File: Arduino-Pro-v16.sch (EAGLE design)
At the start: 42 parts, among them IC1 ATMEGA1281-16AU

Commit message: Added FTDI 3.3V programmer
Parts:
- added C4: (no value), SparkFun-Capacitors:CAP0603-CAP
- added J1: FTDI Basic Programmer, SparkFun-Connectors:ARDUINO_SERIAL_PROGRAMPTH
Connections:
- removed net VCCA: PCB1.5V@2, PCB1.5V@4
- new net DTR: C4.2, J1.DTR
- new net RXI: IC1.(RXD1/INT2)PD2, J1.TXO
- new net TX0: IC1.(TXD1/INT3)PD3, J1.RXI
- net 3V3: now also J1.VCC, PCB1.3V3@1, PCB1.3V3@17
- net 5VMISO: now also JP3.1
- net 5VMOSI: now also JP3.4
- net 5VROV: now also PCB1.5V@2, PCB1.5V@4
- net 5VSCK: now also JP3.3
- net GND: now also J1.CTS, J1.GND
- net MISO: no longer JP3.1
- net MOSI: no longer JP3.4
- net RESET: now also C4.1
- net SCK: no longer JP3.3
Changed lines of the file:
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@@
 <part name="U$1" library="DiscreteComponents" deviceset="SWITCH" device=""/>
 <part name="JTAG_CONNECTOR" library="Connectors" deviceset="MICRO-FIT-4-SMD" device="" technology="-PART"/>
+<part name="3V1" library="SparkFun-Aesthetics" deviceset="VCCA" device=""/>
+<part name="3V4" library="SparkFun-Aesthetics" deviceset="VCCA" device=""/>
+<part name="J1" library="SparkFun-Connectors" deviceset="ARDUINO_SERIAL_PROGRAM" device="PTH" value="FTDI Basic Programmer"/>
+<part name="C4" library="SparkFun-Capacitors" deviceset="CAP" device="0603-CAP"/>
 </parts>
 <sheets>
@@
 <instance part="U$1" gate="G$1" x="-218.44" y="149.86" rot="R90"/>
 <instance part="JTAG_CONNECTOR" gate="G$1" x="-104.14" y="43.18" rot="R270"/>
+<instance part="3V1" gate="G$1" x="302.26" y="127" smashed="yes"/>
+<instance part="3V4" gate="G$1" x="342.9" y="119.38" smashed="yes"/>
+<instance part="J1" gate="G$1" x="137.16" y="137.16"/>
+<instance part="C4" gate="G$1" x="-231.14" y="160.02" rot="R270"/>
 </instances>
 <busses>
@@
 <wire x1="-218.44" y1="142.24" x2="-218.44" y2="139.7" width="0.1524" layer="91"/>
 </segment>
+<segment>
+<pinref part="J1" gate="G$1" pin="GND"/>
+<wire x1="142.24" y1="144.78" x2="147.32" y2="144.78" width="0.1524" layer="91"/>
+<label x="142.24" y="144.78" size="1.778" layer="95"/>
+</segment>
+<segment>
+<pinref part="J1" gate="G$1" pin="CTS"/>
+<wire x1="142.24" y1="142.24" x2="147.32" y2="142.24" width="0.1524" layer="91"/>
+<label x="142.24" y="142.24" size="1.778" layer="95"/>
+</segment>
 </net>
 <net name="RESET" class="0">
@@
 <wire x1="-218.44" y1="160.02" x2="-218.44" y2="157.48" width="0.1524" layer="91"/>
 <junction x="-218.44" y="160.02"/>
+<pinref part="C4" gate="G$1" pin="1"/>
+<wire x1="-226.06" y1="160.02" x2="-218.44" y2="160.02" width="0.1524" layer="91"/>
 </segment>
 </net>
 <net name="SCK" class="0">
-<segment>
-<wire x1="30.48" y1="144.78" x2="15.24" y2="144.78" width="0.1524" layer="91"/>
-<label x="15.24" y="144.78" size="1.778" layer="95"/>
-<pinref part="JP3" gate="G$1" pin="3"/>
-</segment>
 <segment>
 <pinref part="SPI_PIN" gate="G$1" pin="4"/>
@@
 <net name="MISO" class="0">
 <segment>
-<wire x1="30.48" y1="147.32" x2="15.24" y2="147.32" width="0.1524" layer="91"/>
-<label x="15.24" y="147.32" size="1.778" layer="95"/>
-<pinref part="JP3" gate="G$1" pin="1"/>
-</segment>
-<segment>
 <pinref part="SPI_PIN" gate="G$1" pin="2"/>
 <wire x1="218.44" y1="137.16" x2="213.36" y2="137.16" width="0.1524" layer="91"/>
@@
 </net>
 <net name="MOSI" class="0">
-<segment>
-<wire x1="48.26" y1="144.78" x2="58.42" y2="144.78" width="0.1524" layer="91"/>
-<label x="53.34" y="144.78" size="1.778" layer="95"/>
-<pinref part="JP3" gate="G$1" pin="4"/>
-</segment>
 <segment>
 <pinref part="SPI_PIN" gate="G$1" pin="3"/>
@@
 <junction x="88.9" y="154.94"/>
 </segment>
+<segment>
+<pinref part="PCB1" gate="G$1" pin="5V@2"/>
+<wire x1="309.88" y1="154.94" x2="309.88" y2="162.56" width="0.1524" layer="91"/>
+<pinref part="5VROV1" gate="G$1" pin="VCCA"/>
+<wire x1="309.88" y1="162.56" x2="312.42" y2="162.56" width="0.1524" layer="91"/>
+<pinref part="PCB1" gate="G$1" pin="5V@4"/>
+<wire x1="312.42" y1="162.56" x2="314.96" y2="162.56" width="0.1524" layer="91"/>
+<wire x1="314.96" y1="162.56" x2="314.96" y2="154.94" width="0.1524" layer="91"/>
+<junction x="312.42" y="162.56"/>
+<label x="304.8" y="162.56" size="1.778" layer="95"/>
+</segment>
 </net>
 <net name="5VPROGRAMMER" class="0">
@@
 <wire x1="-116.84" y1="124.46" x2="-109.22" y2="124.46" width="0.1524" layer="91"/>
 <label x="-114.3" y="124.46" size="1.778" layer="95"/>
+</segment>
+<segment>
+<wire x1="48.26" y1="144.78" x2="58.42" y2="144.78" width="0.1524" layer="91"/>
+<label x="53.34" y="144.78" size="1.778" layer="95"/>
+<pinref part="JP3" gate="G$1" pin="4"/>
 </segment>
 </net>
@@
 <label x="45.72" y="66.04" size="1.778" layer="95" rot="R180"/>
 </segment>
+<segment>
+<pinref part="3V1" gate="G$1" pin="VCCA"/>
+<pinref part="PCB1" gate="G$1" pin="3V3@1"/>
+<wire x1="302.26" y1="127" x2="309.88" y2="127" width="0.1524" layer="91"/>
+<label x="302.26" y="124.46" size="1.778" layer="95"/>
+</segment>
+<segment>
+<pinref part="3V4" gate="G$1" pin="VCCA"/>
+<pinref part="PCB1" gate="G$1" pin="3V3@17"/>
+<wire x1="342.9" y1="119.38" x2="350.52" y2="119.38" width="0.1524" layer="91"/>
+<wire x1="350.52" y1="119.38" x2="350.52" y2="127" width="0.1524" layer="91"/>
+<label x="342.9" y="116.84" size="1.778" layer="95"/>
+</segment>
+<segment>
+<pinref part="J1" gate="G$1" pin="VCC"/>
+<wire x1="142.24" y1="139.7" x2="147.32" y2="139.7" width="0.1524" layer="91"/>
+<label x="142.24" y="139.7" size="1.778" layer="95"/>
+</segment>
 </net>
 <net name="3V3MOSI" class="0">
@@
 <label x="-114.3" y="127" size="1.778" layer="95"/>
 </segment>
+<segment>
+<wire x1="30.48" y1="147.32" x2="15.24" y2="147.32" width="0.1524" layer="91"/>
+<label x="15.24" y="147.32" size="1.778" layer="95"/>
+<pinref part="JP3" gate="G$1" pin="1"/>
+</segment>
 </net>
 <net name="5VSCK" class="0">
@@
 <label x="-114.3" y="121.92" size="1.778" layer="95"/>
 </segment>
-</net>
-<net name="VCCA" class="0">
-<segment>
-<pinref part="PCB1" gate="G$1" pin="5V@2"/>
-<wire x1="309.88" y1="154.94" x2="309.88" y2="162.56" width="0.1524" layer="91"/>
-<pinref part="5VROV1" gate="G$1" pin="VCCA"/>
-<wire x1="309.88" y1="162.56" x2="312.42" y2="162.56" width="0.1524" layer="91"/>
-<pinref part="PCB1" gate="G$1" pin="5V@4"/>
-<wire x1="312.42" y1="162.56" x2="314.96" y2="162.56" width="0.1524" layer="91"/>
-<wire x1="314.96" y1="162.56" x2="314.96" y2="154.94" width="0.1524" layer="91"/>
-<junction x="312.42" y="162.56"/>
+<segment>
+<wire x1="30.48" y1="144.78" x2="15.24" y2="144.78" width="0.1524" layer="91"/>
+<label x="15.24" y="144.78" size="1.778" layer="95"/>
+<pinref part="JP3" gate="G$1" pin="3"/>
 </segment>
 </net>
@@
 </segment>
 </net>
+<net name="RXI" class="0">
+<segment>
+<pinref part="IC1" gate="G$1" pin="(RXD1/INT2)PD2"/>
+<wire x1="-116.84" y1="78.74" x2="-111.76" y2="78.74" width="0.1524" layer="91"/>
+<label x="-116.84" y="78.74" size="1.778" layer="95"/>
+</segment>
+<segment>
+<pinref part="J1" gate="G$1" pin="TXO"/>
+<wire x1="142.24" y1="137.16" x2="147.32" y2="137.16" width="0.1524" layer="91"/>
+<label x="142.24" y="137.16" size="1.778" layer="95"/>
+</segment>
+</net>
+<net name="TX0" class="0">
+<segment>
+<pinref part="IC1" gate="G$1" pin="(TXD1/INT3)PD3"/>
+<wire x1="-116.84" y1="81.28" x2="-111.76" y2="81.28" width="0.1524" layer="91"/>
+<label x="-116.84" y="81.28" size="1.778" layer="95"/>
+</segment>
+<segment>
+<pinref part="J1" gate="G$1" pin="RXI"/>
+<wire x1="142.24" y1="134.62" x2="147.32" y2="134.62" width="0.1524" layer="91"/>
+<label x="142.24" y="134.62" size="1.778" layer="95"/>
+</segment>
+</net>
+<net name="DTR" class="0">
+<segment>
+<pinref part="C4" gate="G$1" pin="2"/>
+<wire x1="-233.68" y1="160.02" x2="-238.76" y2="160.02" width="0.1524" layer="91"/>
+<label x="-238.76" y="160.02" size="1.778" layer="95"/>
+</segment>
+<segment>
+<pinref part="J1" gate="G$1" pin="DTR"/>
+<wire x1="142.24" y1="132.08" x2="147.32" y2="132.08" width="0.1524" layer="91"/>
+<label x="142.24" y="132.08" size="1.778" layer="95"/>
+</segment>
+</net>

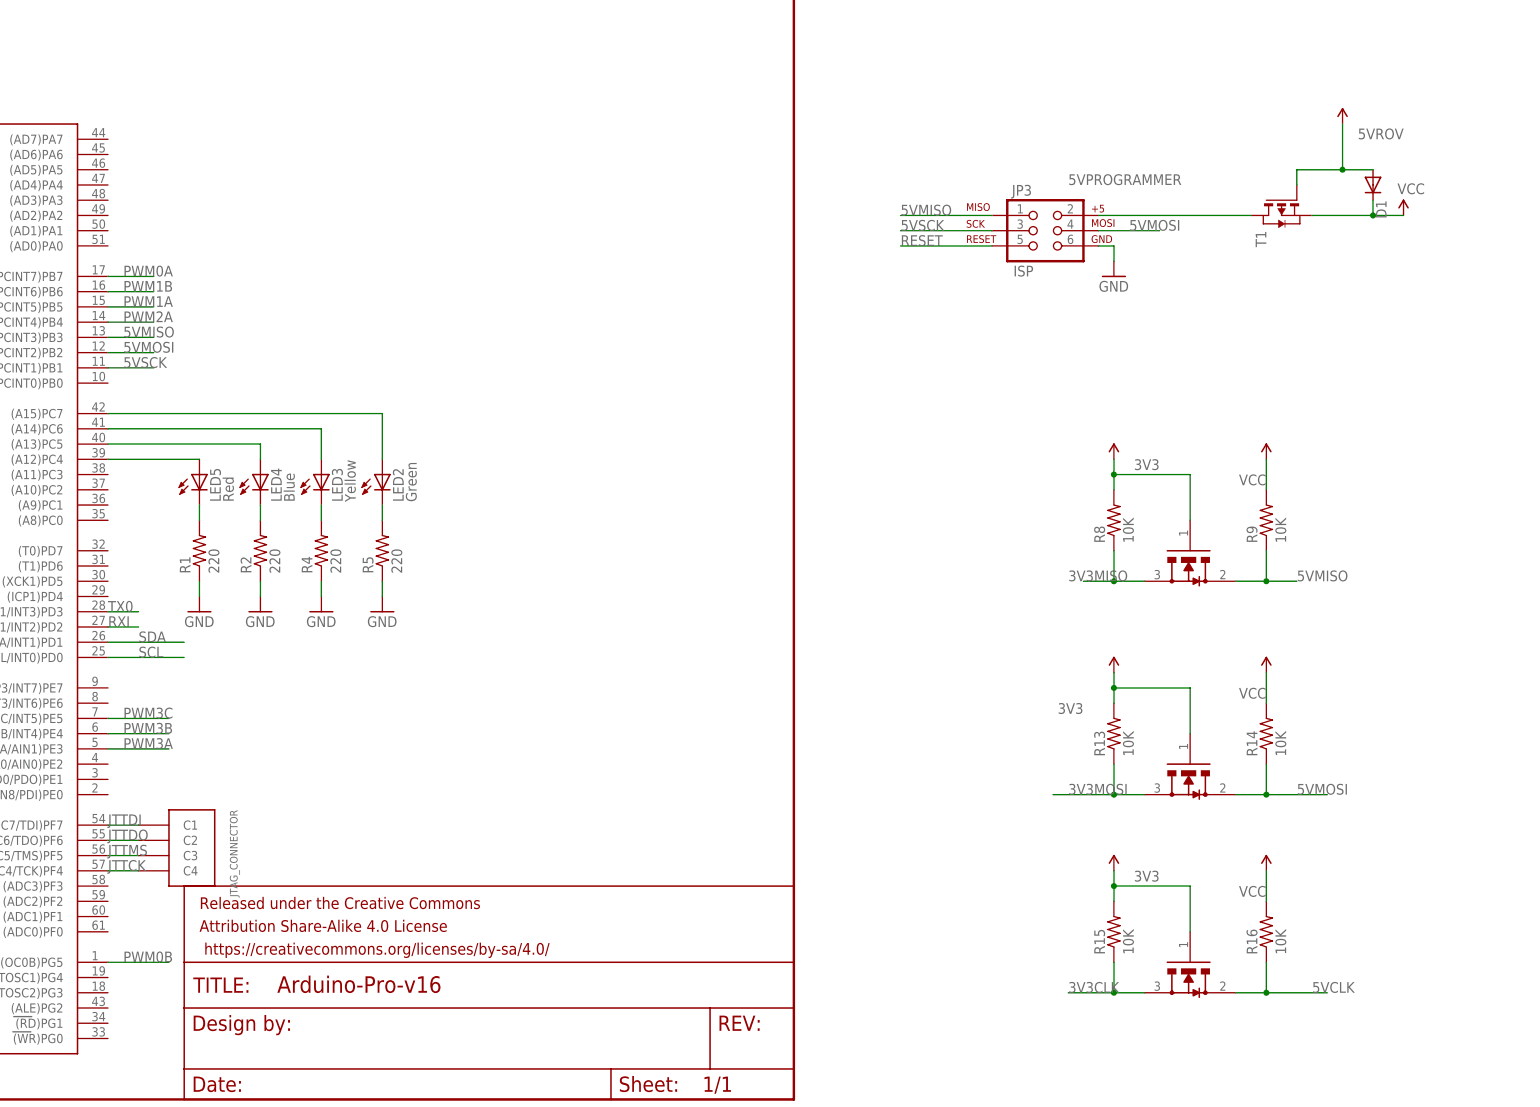
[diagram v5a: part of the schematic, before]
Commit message: Added 3.3V linear regulator, delete logic level shifters
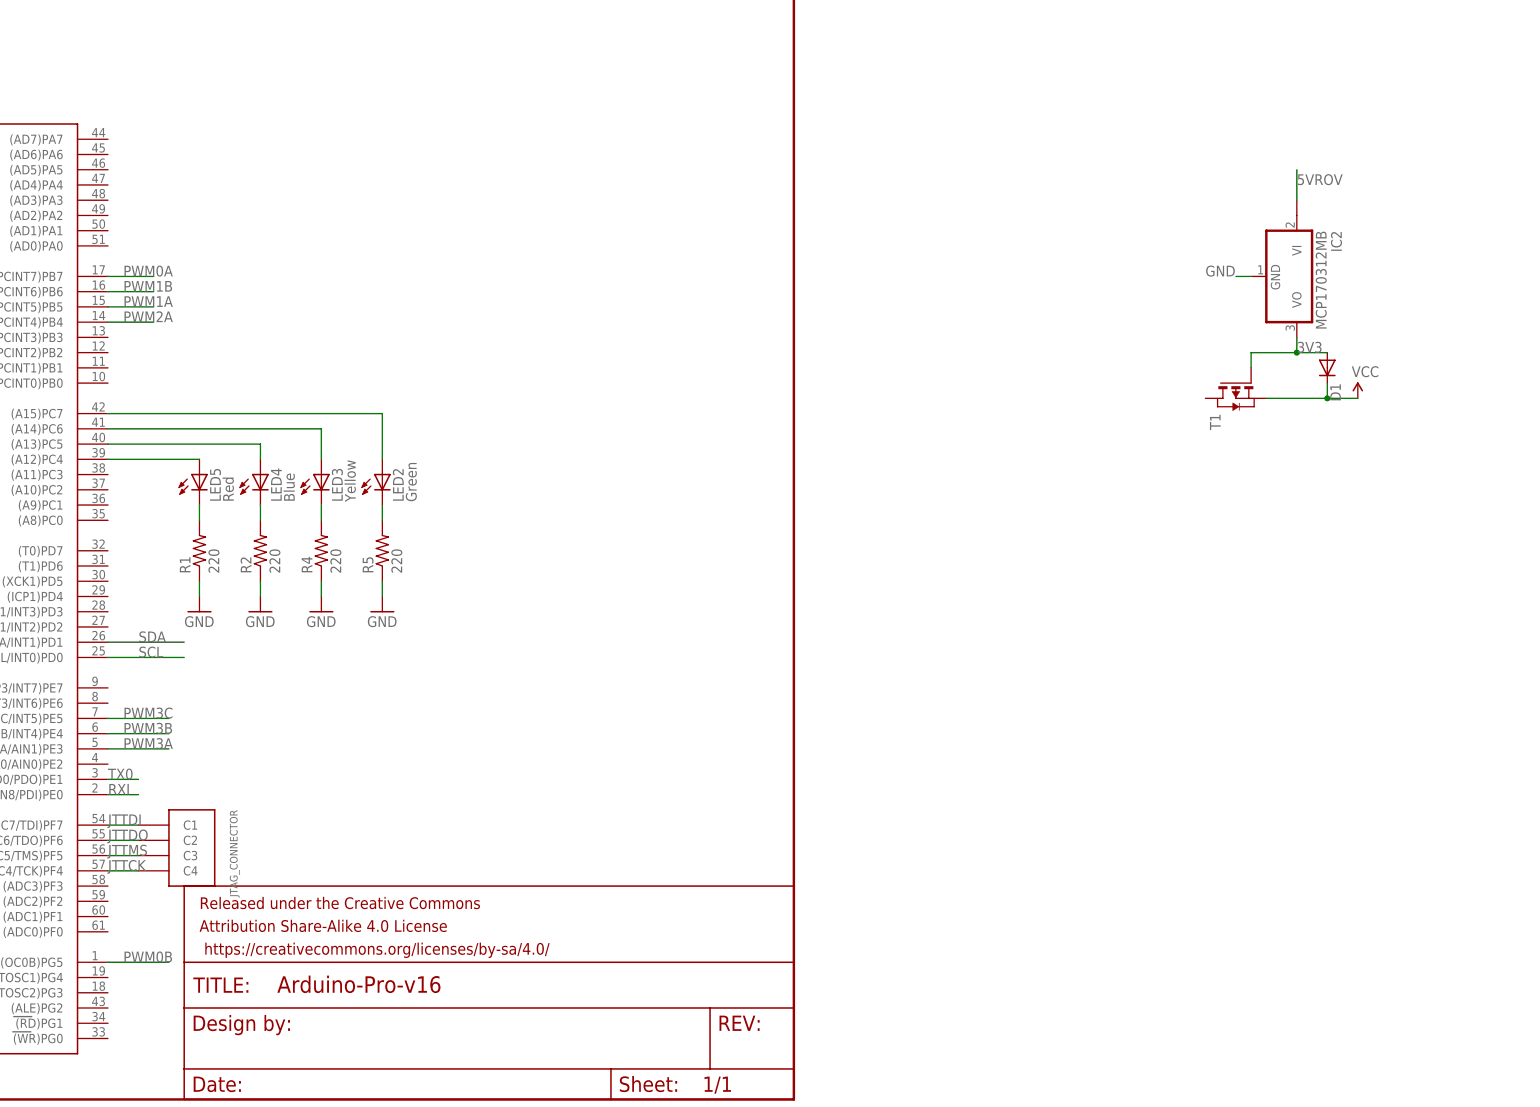
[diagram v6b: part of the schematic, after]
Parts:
- removed JP3: ISP, SparkFun:AVR_SPI_PRG_6PTH
- removed R13, R14, R15, R16, R8, R9: 10K, SparkFun:RESISTOR0402-RES
- removed U$3, U$4, U$6: BSS138, DiscreteComponents:BSS138
- added IC2: MCP170312MB, linear:MCP170312MB
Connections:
- removed net 5VCLK: R16.1, U$6.D
- removed net 5VMISO: IC1.(MISO/PCINT3)PB3, JP3.1, R9.1, U$3.D
- removed net 5VMOSI: IC1.(MOSI/PCINT2)PB2, JP3.4, R14.1, U$4.D
- removed net 5VPROGRAMMER: JP3.2, T1.D
- removed net 5VSCK: IC1.(SCK/PCINT1)PB1, JP3.3
- net 3V3: now also D1.A, IC2.VO, T1.G; no longer R13.2, R15.2, R8.2, U$3.G, U$4.G, U$6.G
- net 3V3CLK: no longer R15.1, U$6.S
- net 3V3MISO: no longer R8.1, U$3.S
- net 3V3MOSI: no longer R13.1, U$4.S
- net 5VROV: now also IC2.VI1; no longer D1.A, T1.G
- net GND: now also IC2.GND; no longer JP3.6
- net RESET: no longer JP3.5
- net RXI: now also IC1.(RXD0/PCIN8/PDI)PE0; no longer IC1.(RXD1/INT2)PD2
- net TX0: now also IC1.(TXD0/PDO)PE1; no longer IC1.(TXD1/INT3)PD3
- net VCC: no longer R14.2, R16.2, R9.2
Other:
- moved on the sheet: D1, T1

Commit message: Added a pin out for alternate 3.3V power supply
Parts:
- added J2: (no value), SparkFun-Connectors:M01PTH
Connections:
- new net ALTVCC: J2.1, T1.D
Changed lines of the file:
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@@
 <part name="C4" library="SparkFun-Capacitors" deviceset="CAP" device="0603-CAP"/>
 <part name="IC2" library="linear" deviceset="MCP1703*" device="MB" technology="12"/>
+<part name="J2" library="SparkFun-Connectors" deviceset="M01" device="PTH"/>
 </parts>
 <sheets>
@@
 <instance part="C4" gate="G$1" x="-231.14" y="160.02" rot="R270"/>
 <instance part="IC2" gate="G$1" x="81.28" y="137.16" rot="R270"/>
+<instance part="J2" gate="G$1" x="43.18" y="116.84"/>
 </instances>
 <busses>
@@
 </segment>
 </net>
+<net name="ALTVCC" class="0">
+<segment>
+<pinref part="T1" gate="A" pin="D"/>
+<label x="55.88" y="116.84" size="1.778" layer="95"/>
+<pinref part="J2" gate="G$1" pin="1"/>
+<wire x1="50.8" y1="116.84" x2="66.04" y2="116.84" width="0.1524" layer="91"/>
+</segment>
+</net>
